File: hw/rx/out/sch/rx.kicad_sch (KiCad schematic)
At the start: 0 parts

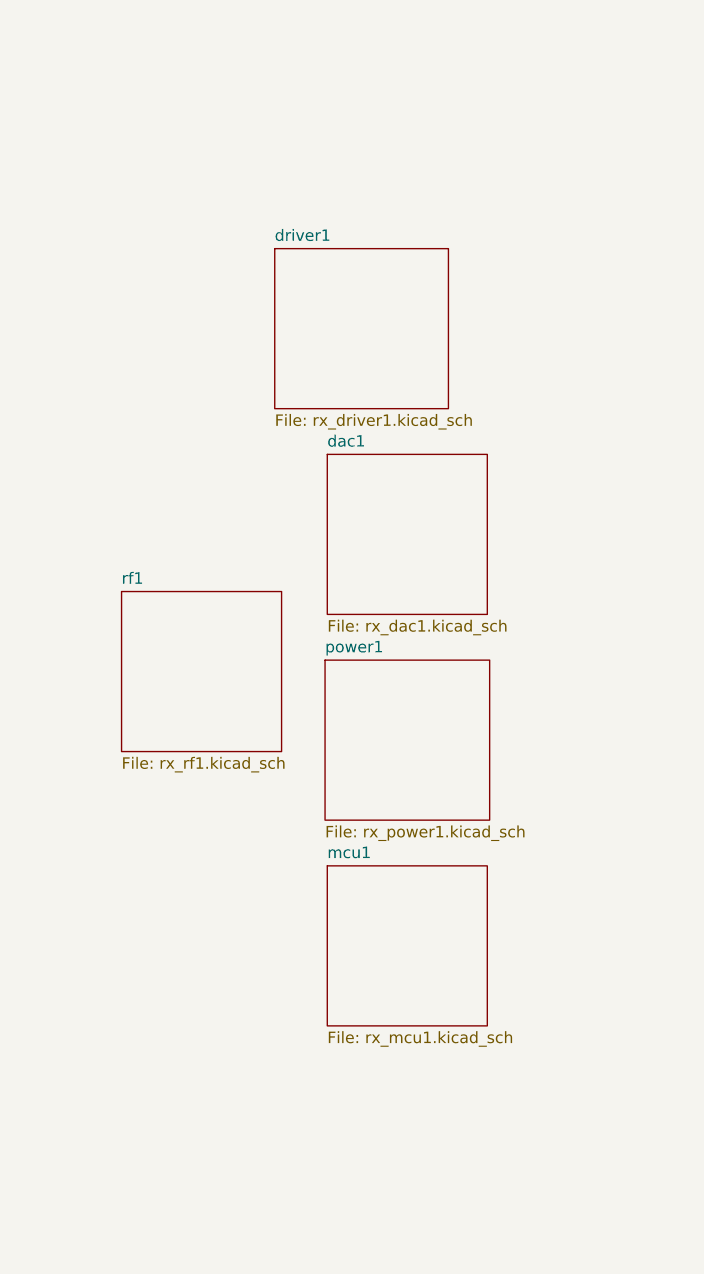
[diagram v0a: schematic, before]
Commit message: hw/rx: review fixes for #81 (mute relay + supervisor, S1J clamps, VCM discharge + 2-pole filter, 16 V LDOs, keyed header, I2S DNP, cable stability + power-cycle SPICE, FLT low latency) (#32)
Co-Authored-By: Claude Opus 5.5 <noreply@anthropic.com>
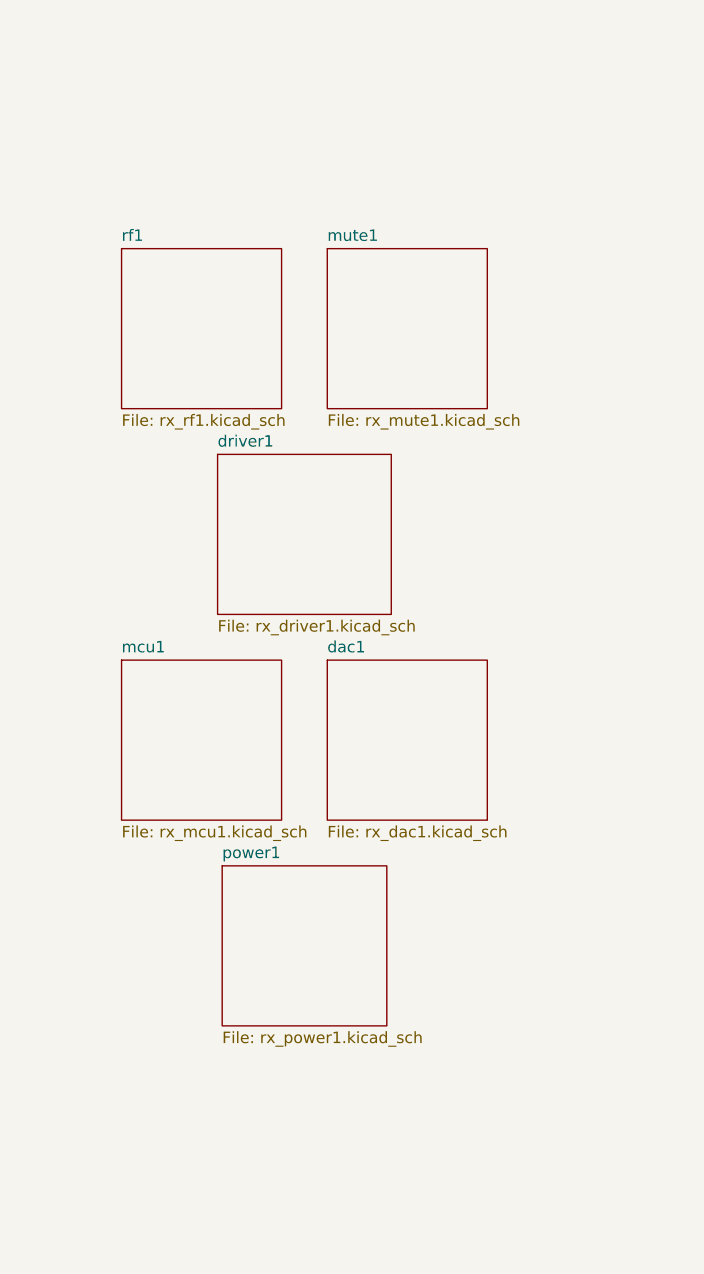
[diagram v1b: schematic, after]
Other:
- added sheet mute1 (rx_mute1.kicad_sch)
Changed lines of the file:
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@@
     (comment 4 ""))
   (sheet
-    (at 150.88 107.95)
+    (at 139.45 130.81)
     (size 18.29 17.78)
     (exclude_from_sim no)
@@
       (color 0 0 0 0.0))
     (property "Sheetname" "power1"
-      (at 150.88 107.24 0)
+      (at 139.45 130.1 0)
       (effects
         (font
@@
         (justify left bottom)))
     (property "Sheetfile" "rx_power1.kicad_sch"
-      (at 150.88 126.31 0)
+      (at 139.45 149.17 0)
       (effects
         (font
@@
         (justify left top))))
   (sheet
-    (at 151.13 130.81)
+    (at 128.27 107.95)
     (size 17.78 17.78)
     (exclude_from_sim no)
@@
       (color 0 0 0 0.0))
     (property "Sheetname" "mcu1"
-      (at 151.13 130.1 0)
+      (at 128.27 107.24 0)
       (effects
         (font
@@
         (justify left bottom)))
     (property "Sheetfile" "rx_mcu1.kicad_sch"
-      (at 151.13 149.17 0)
+      (at 128.27 126.31 0)
       (effects
         (font
@@
         (justify left top))))
   (sheet
-    (at 128.27 100.33)
+    (at 128.27 62.23)
     (size 17.78 17.78)
     (exclude_from_sim no)
@@
       (color 0 0 0 0.0))
     (property "Sheetname" "rf1"
-      (at 128.27 99.62 0)
+      (at 128.27 61.52 0)
       (effects
         (font
@@
         (justify left bottom)))
     (property "Sheetfile" "rx_rf1.kicad_sch"
-      (at 128.27 118.69 0)
+      (at 128.27 80.59 0)
       (effects
         (font
@@
         (justify left top))))
   (sheet
-    (at 151.13 85.09)
+    (at 151.13 107.95)
     (size 17.78 17.78)
     (exclude_from_sim no)
@@
       (color 0 0 0 0.0))
     (property "Sheetname" "dac1"
-      (at 151.13 84.38 0)
+      (at 151.13 107.24 0)
       (effects
         (font
@@
         (justify left bottom)))
     (property "Sheetfile" "rx_dac1.kicad_sch"
-      (at 151.13 103.45 0)
+      (at 151.13 126.31 0)
       (effects
         (font
@@
         (justify left top))))
   (sheet
-    (at 145.29 62.23)
+    (at 138.94 85.09)
     (size 19.3 17.78)
     (exclude_from_sim no)
@@
       (color 0 0 0 0.0))
     (property "Sheetname" "driver1"
-      (at 145.29 61.52 0)
+      (at 138.94 84.38 0)
       (effects
         (font
@@
         (justify left bottom)))
     (property "Sheetfile" "rx_driver1.kicad_sch"
-      (at 145.29 80.59 0)
+      (at 138.94 103.45 0)
       (effects
         (font
+          (size 1.27 1.27))
+        (justify left top))))
+  (sheet
+    (at 151.13 62.23)
+    (size 17.78 17.78)
+    (exclude_from_sim no)
+    (in_bom yes)
+    (on_board yes)
+    (dnp no)
+    (fields_autoplaced yes)
+    (stroke
+      (width 0.1524)
+      (type solid))
+    (fill
+      (color 0 0 0 0.0))
+    (property "Sheetname" "mute1"
+      (at 151.13 61.52 0)
+      (effects
+        (font
+          (size 1.27 1.27))
+        (justify left bottom)))
+    (property "Sheetfile" "rx_mute1.kicad_sch"
+      (at 151.13 80.59 0)
+      (effects
+        (font

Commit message: hw/rx: receiver module BT40NE -> BT40E, FEM node pack-only (ADR-0021, #112)
- hw/rx: BT40E symbol (Fanstel v1.09 p.14 pad map = BT40F/NE names), footprint
  openpack:Fanstel_BT40E (14x16 mm), no FEM nets, P1.05 open; GPIO map unchanged.
  ERC 0/0. BOM: Digi-Key UK GBP 9.7765 q100 -> $30.68 / GBP 23.38 per sub-board.
- fw: receiver builds add boards/role_rx_cpunet.overlay (FEM node disabled, no
  &radio fem); rx.c refuses to build with the FEM enabled.
- ADR-0014 amended (datasheet checks, FCC X8WBT40F, no UKCA DoC, BOM).

Co-Authored-By: Claude Opus 5.5 <noreply@anthropic.com>
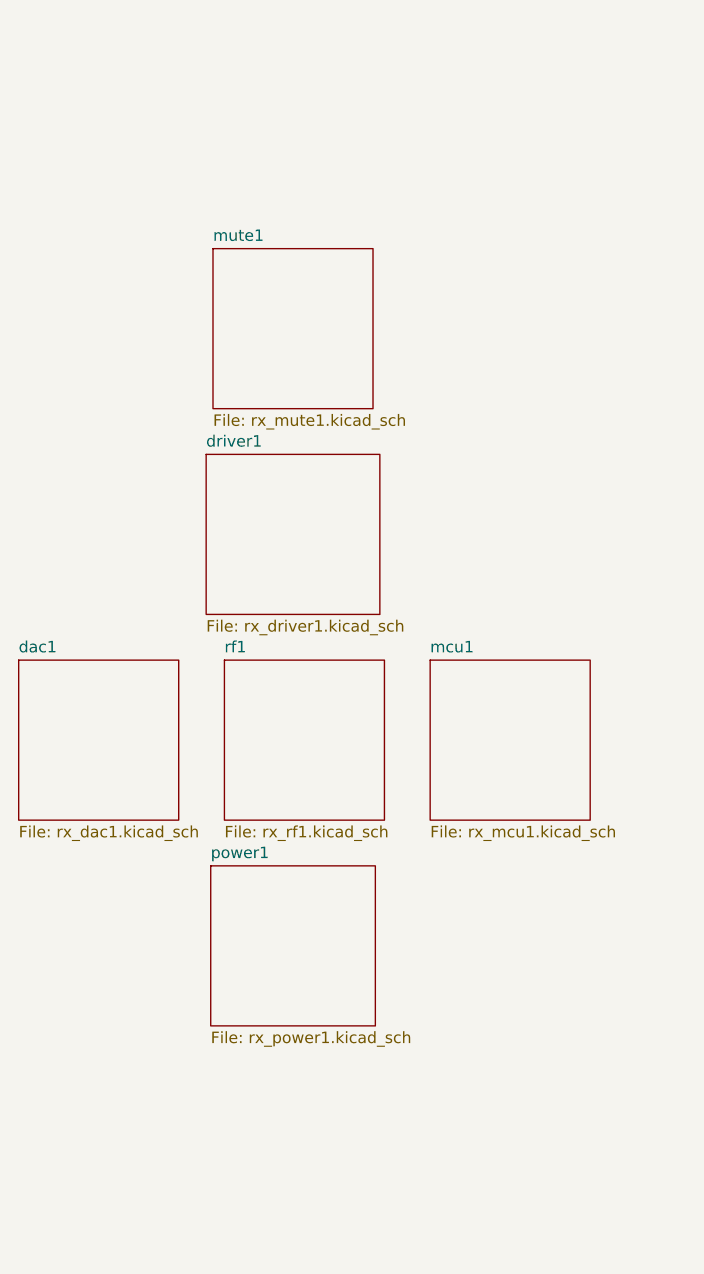
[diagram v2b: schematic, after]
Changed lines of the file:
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@@
   (title_block
     (title "OpenPack receiver sub-board")
-    (date "2026-10-31")
+    (date "2026-11-01")
     (company "")
     (comment 1 "Generated with SKiDL")
@@
     (comment 4 ""))
   (sheet
-    (at 139.45 130.81)
+    (at 138.18 130.81)
     (size 18.29 17.78)
     (exclude_from_sim no)
@@
       (color 0 0 0 0.0))
     (property "Sheetname" "power1"
-      (at 139.45 130.1 0)
+      (at 138.18 130.1 0)
       (effects
         (font
@@
         (justify left bottom)))
     (property "Sheetfile" "rx_power1.kicad_sch"
-      (at 139.45 149.17 0)
+      (at 138.18 149.17 0)
       (effects
         (font
@@
         (justify left top))))
   (sheet
-    (at 128.27 107.95)
+    (at 162.56 107.95)
     (size 17.78 17.78)
     (exclude_from_sim no)
@@
       (color 0 0 0 0.0))
     (property "Sheetname" "mcu1"
-      (at 128.27 107.24 0)
+      (at 162.56 107.24 0)
       (effects
         (font
@@
         (justify left bottom)))
     (property "Sheetfile" "rx_mcu1.kicad_sch"
-      (at 128.27 126.31 0)
+      (at 162.56 126.31 0)
       (effects
         (font
@@
         (justify left top))))
   (sheet
-    (at 128.27 62.23)
+    (at 139.7 107.95)
     (size 17.78 17.78)
     (exclude_from_sim no)
@@
       (color 0 0 0 0.0))
     (property "Sheetname" "rf1"
-      (at 128.27 61.52 0)
+      (at 139.7 107.24 0)
       (effects
         (font
@@
         (justify left bottom)))
     (property "Sheetfile" "rx_rf1.kicad_sch"
-      (at 128.27 80.59 0)
+      (at 139.7 126.31 0)
       (effects
         (font
@@
         (justify left top))))
   (sheet
-    (at 151.13 107.95)
+    (at 116.84 107.95)
     (size 17.78 17.78)
     (exclude_from_sim no)
@@
       (color 0 0 0 0.0))
     (property "Sheetname" "dac1"
-      (at 151.13 107.24 0)
+      (at 116.84 107.24 0)
       (effects
         (font
@@
         (justify left bottom)))
     (property "Sheetfile" "rx_dac1.kicad_sch"
-      (at 151.13 126.31 0)
+      (at 116.84 126.31 0)
       (effects
         (font
@@
         (justify left top))))
   (sheet
-    (at 138.94 85.09)
+    (at 137.67 85.09)
     (size 19.3 17.78)
     (exclude_from_sim no)
@@
       (color 0 0 0 0.0))
     (property "Sheetname" "driver1"
-      (at 138.94 84.38 0)
+      (at 137.67 84.38 0)
       (effects
         (font
@@
         (justify left bottom)))
     (property "Sheetfile" "rx_driver1.kicad_sch"
-      (at 138.94 103.45 0)
+      (at 137.67 103.45 0)
       (effects
         (font
@@
         (justify left top))))
   (sheet
-    (at 151.13 62.23)
+    (at 138.43 62.23)
     (size 17.78 17.78)
     (exclude_from_sim no)
@@
       (color 0 0 0 0.0))
     (property "Sheetname" "mute1"
-      (at 151.13 61.52 0)
+      (at 138.43 61.52 0)
       (effects
         (font
@@
         (justify left bottom)))
     (property "Sheetfile" "rx_mute1.kicad_sch"
-      (at 151.13 80.59 0)
+      (at 138.43 80.59 0)
       (effects
         (font

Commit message: hw/rx: BT40E + TQ2SA footprints, THT underside backplane header, bring-up test points (#34)
Co-Authored-By: Claude Opus 5.5 <noreply@anthropic.com>
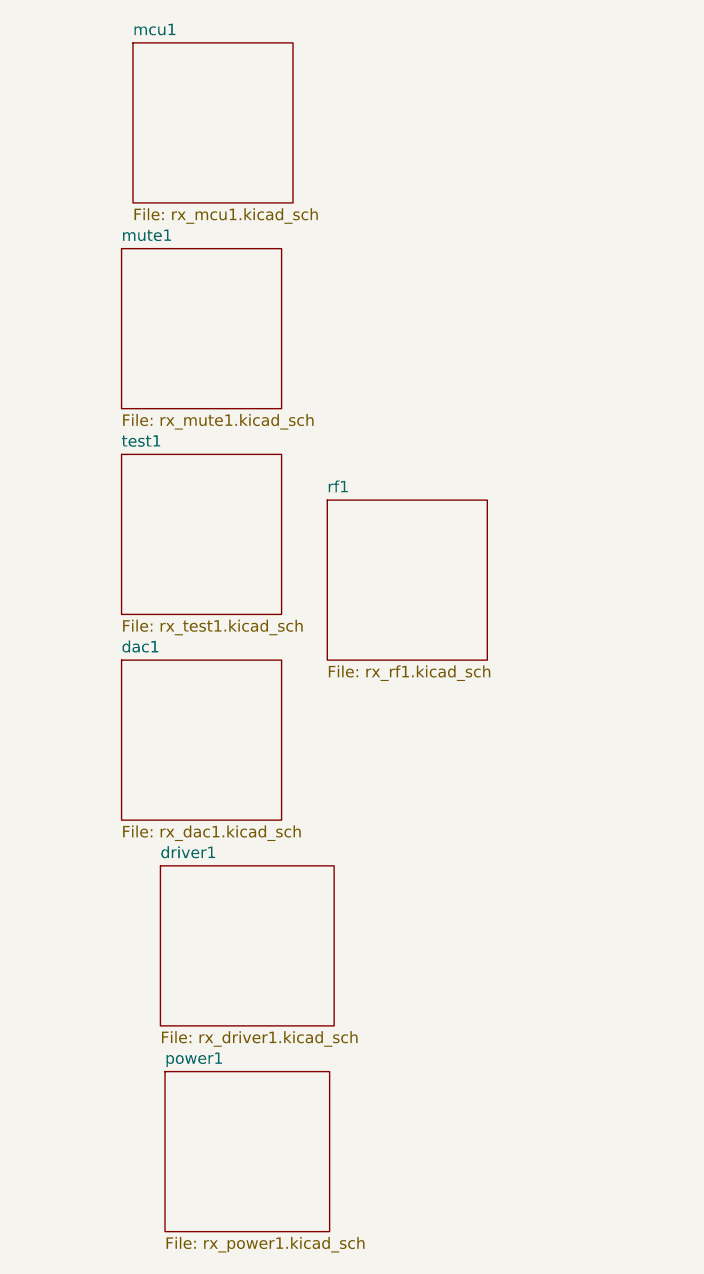
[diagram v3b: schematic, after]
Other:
- added sheet test1 (rx_test1.kicad_sch)
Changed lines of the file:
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@@
     (comment 4 ""))
   (sheet
-    (at 138.18 130.81)
+    (at 133.1 153.67)
     (size 18.29 17.78)
     (exclude_from_sim no)
@@
       (color 0 0 0 0.0))
     (property "Sheetname" "power1"
-      (at 138.18 130.1 0)
+      (at 133.1 152.96 0)
       (effects
         (font
@@
         (justify left bottom)))
     (property "Sheetfile" "rx_power1.kicad_sch"
-      (at 138.18 149.17 0)
+      (at 133.1 172.03 0)
       (effects
         (font
@@
         (justify left top))))
   (sheet
-    (at 162.56 107.95)
+    (at 129.54 39.37)
     (size 17.78 17.78)
     (exclude_from_sim no)
@@
       (color 0 0 0 0.0))
     (property "Sheetname" "mcu1"
-      (at 162.56 107.24 0)
+      (at 129.54 38.66 0)
       (effects
         (font
@@
         (justify left bottom)))
     (property "Sheetfile" "rx_mcu1.kicad_sch"
-      (at 162.56 126.31 0)
+      (at 129.54 57.73 0)
       (effects
         (font
@@
         (justify left top))))
   (sheet
-    (at 139.7 107.95)
+    (at 151.13 90.17)
     (size 17.78 17.78)
     (exclude_from_sim no)
@@
       (color 0 0 0 0.0))
     (property "Sheetname" "rf1"
-      (at 139.7 107.24 0)
+      (at 151.13 89.46 0)
       (effects
         (font
@@
         (justify left bottom)))
     (property "Sheetfile" "rx_rf1.kicad_sch"
-      (at 139.7 126.31 0)
+      (at 151.13 108.53 0)
       (effects
         (font
@@
         (justify left top))))
   (sheet
-    (at 116.84 107.95)
+    (at 128.27 107.95)
     (size 17.78 17.78)
     (exclude_from_sim no)
@@
       (color 0 0 0 0.0))
     (property "Sheetname" "dac1"
-      (at 116.84 107.24 0)
+      (at 128.27 107.24 0)
       (effects
         (font
@@
         (justify left bottom)))
     (property "Sheetfile" "rx_dac1.kicad_sch"
-      (at 116.84 126.31 0)
+      (at 128.27 126.31 0)
       (effects
         (font
@@
         (justify left top))))
   (sheet
-    (at 137.67 85.09)
+    (at 132.59 130.81)
     (size 19.3 17.78)
     (exclude_from_sim no)
@@
       (color 0 0 0 0.0))
     (property "Sheetname" "driver1"
-      (at 137.67 84.38 0)
+      (at 132.59 130.1 0)
       (effects
         (font
@@
         (justify left bottom)))
     (property "Sheetfile" "rx_driver1.kicad_sch"
-      (at 137.67 103.45 0)
+      (at 132.59 149.17 0)
       (effects
         (font
@@
         (justify left top))))
   (sheet
-    (at 138.43 62.23)
+    (at 128.27 62.23)
     (size 17.78 17.78)
     (exclude_from_sim no)
@@
       (color 0 0 0 0.0))
     (property "Sheetname" "mute1"
-      (at 138.43 61.52 0)
+      (at 128.27 61.52 0)
       (effects
         (font
@@
         (justify left bottom)))
     (property "Sheetfile" "rx_mute1.kicad_sch"
-      (at 138.43 80.59 0)
+      (at 128.27 80.59 0)
       (effects
         (font
+          (size 1.27 1.27))
+        (justify left top))))
+  (sheet
+    (at 128.27 85.09)
+    (size 17.78 17.78)
+    (exclude_from_sim no)
+    (in_bom yes)
+    (on_board yes)
+    (dnp no)
+    (fields_autoplaced yes)
+    (stroke
+      (width 0.1524)
+      (type solid))
+    (fill
+      (color 0 0 0 0.0))
+    (property "Sheetname" "test1"
+      (at 128.27 84.38 0)
+      (effects
+        (font
+          (size 1.27 1.27))
+        (justify left bottom)))
+    (property "Sheetfile" "rx_test1.kicad_sch"
+      (at 128.27 103.45 0)
+      (effects
+        (font
